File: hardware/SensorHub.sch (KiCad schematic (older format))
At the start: 38 parts, among them IC1 VEML6070, IC2 LT3652EMSE, IC3 BME680, IC4 BH1726, IC5 MCP9808, M1 ParticleArgon, SW1 ENABLE, X1 WIND, X2 SOLAR

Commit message: Release hardware version 1.2
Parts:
- L1: Mfr. No. IDC2512ER330M -> IDC2512ER220M; Order Number 70-IDC2512ER330M -> 70-IDC2512ER220M
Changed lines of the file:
@@
 F 3 "https://www.mouser.de/datasheet/2/427/idc2512-1762893.pdf" H 3700 2650 50  0001 C CNN
 F 4 "Vishay / Dale" V 3981 2650 50  0001 C CNN "Mfr."
-F 5 "IDC2512ER330M" V 3890 2650 50  0001 C CNN "Mfr. No."
+F 5 "IDC2512ER220M" V 3890 2650 50  0001 C CNN "Mfr. No."
 F 6 "Mouser" H 3700 2650 50  0001 C CNN "Distributor"
-F 7 "70-IDC2512ER330M" H 3700 2650 50  0001 C CNN "Order Number"
+F 7 "70-IDC2512ER220M" H 3700 2650 50  0001 C CNN "Order Number"
 	1    3700 2650
 	0    1    1    0

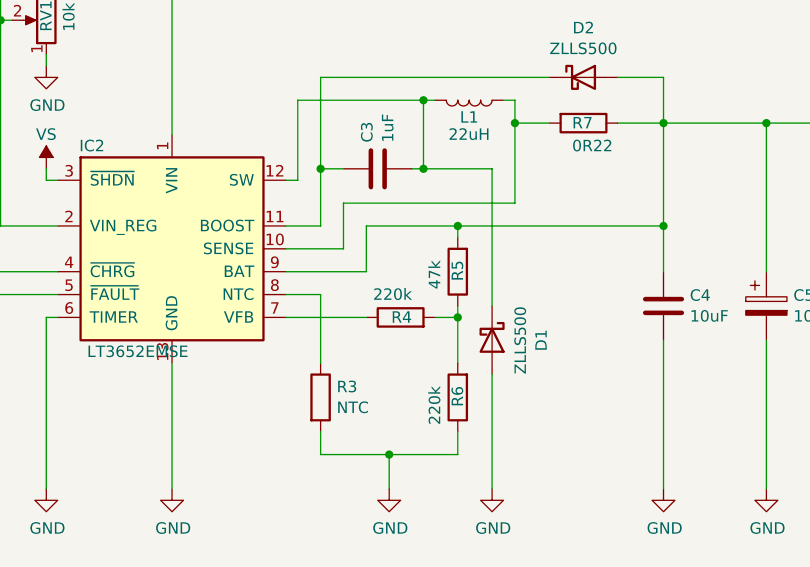
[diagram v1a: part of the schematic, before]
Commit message: - Change the values of the three feedback resistors ('R4', 'R5' and 'R6')
Signed-off-by: Daniel Kampert <DanielKampert@kampis-elektroecke.de>
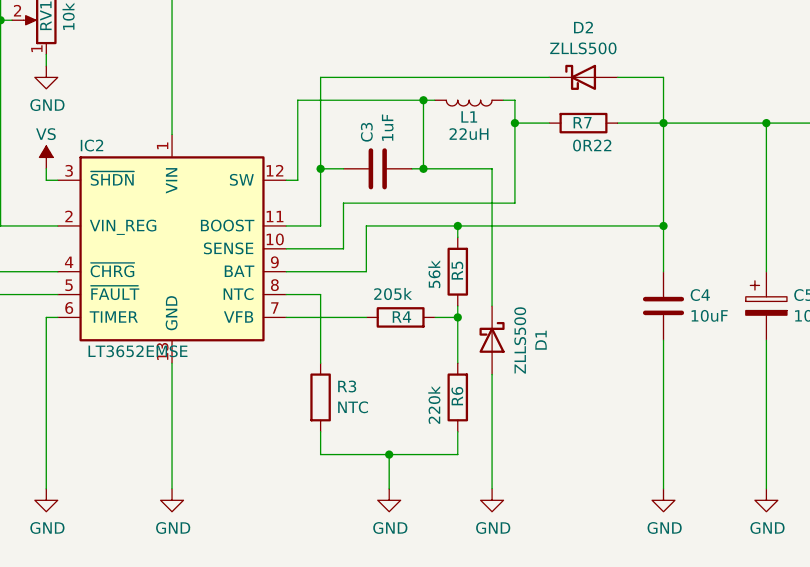
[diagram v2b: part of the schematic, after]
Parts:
- R4: value 220k -> 205k; Mfr. TE Connectivity -> Rohm Semiconductor; Mfr. No. CRGP0805F220K -> KTR10EZPF2053; Order Number 279-CRGP0805F220K -> 755-KTR10EZPF2053
- R5: value 47k -> 56k; Mfr. TE Connectivity -> Rohm Semiconductor; Mfr. No. CRGP0805F47K -> KTR10EZPF5602; Order Number 279-CRGP0805F47K -> 755-KTR10EZPF5602
- R6: Mfr. TE Connectivity -> Bourns; Mfr. No. CRGP0805F220K -> CHV0805-FX-2203ELF; Order Number 279-CRGP0805F220K -> 652-CHV0805FX2203ELF
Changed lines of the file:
@@
 P 3400 3600
 F 0 "R4" V 3400 3550 50  0000 L CNN
-F 1 "220k" V 3500 3550 50  0000 L CNN
+F 1 "205k" V 3500 3550 50  0000 L CNN
 F 2 "Resistor_SMD:R_0805_2012Metric_Pad1.15x1.40mm_HandSolder" V 3330 3600 50  0001 C CNN
-F 3 "~" H 3400 3600 50  0001 C CNN
-F 4 "TE Connectivity" H 3400 3600 50  0001 C CNN "Mfr."
-F 5 "CRGP0805F220K" H 3400 3600 50  0001 C CNN "Mfr. No."
+F 3 "https://www.mouser.de/datasheet/2/348/ktr-e-1139187.pdf" H 3400 3600 50  0001 C CNN
+F 4 "Rohm Semiconductor" H 3400 3600 50  0001 C CNN "Mfr."
+F 5 "KTR10EZPF2053" H 3400 3600 50  0001 C CNN "Mfr. No."
 F 6 "Mouser" H 3400 3600 50  0001 C CNN "Distributor"
-F 7 "279-CRGP0805F220K" H 3400 3600 50  0001 C CNN "Order Number"
+F 7 "755-KTR10EZPF2053" H 3400 3600 50  0001 C CNN "Order Number"
 	1    3400 3600
 	0    -1   -1   0
@@
 P 3650 3400
 F 0 "R5" V 3650 3350 50  0000 L CNN
-F 1 "47k" V 3750 3350 50  0000 L CNN
+F 1 "56k" V 3750 3350 50  0000 L CNN
 F 2 "Resistor_SMD:R_0805_2012Metric_Pad1.15x1.40mm_HandSolder" V 3580 3400 50  0001 C CNN
-F 3 "~" H 3650 3400 50  0001 C CNN
-F 4 "TE Connectivity" H 3650 3400 50  0001 C CNN "Mfr."
-F 5 "CRGP0805F47K" H 3650 3400 50  0001 C CNN "Mfr. No."
+F 3 "https://www.mouser.de/datasheet/2/348/ktr-e-1139187.pdf" H 3650 3400 50  0001 C CNN
+F 4 "Rohm Semiconductor" H 3650 3400 50  0001 C CNN "Mfr."
+F 5 "KTR10EZPF5602" H 3650 3400 50  0001 C CNN "Mfr. No."
 F 6 "Mouser" H 3650 3400 50  0001 C CNN "Distributor"
-F 7 "279-CRGP0805F47K" H 3650 3400 50  0001 C CNN "Order Number"
+F 7 "755-KTR10EZPF5602" H 3650 3400 50  0001 C CNN "Order Number"
 	1    3650 3400
 	-1   0    0    1
@@
 F 1 "220k" V 3750 3900 50  0000 L CNN
 F 2 "Resistor_SMD:R_0805_2012Metric_Pad1.15x1.40mm_HandSolder" V 3580 3950 50  0001 C CNN
-F 3 "~" H 3650 3950 50  0001 C CNN
-F 4 "TE Connectivity" H 3650 3950 50  0001 C CNN "Mfr."
-F 5 "CRGP0805F220K" H 3650 3950 50  0001 C CNN "Mfr. No."
+F 3 "https://www.mouser.de/ProductDetail/Bourns/CHV0805-FX-2203ELF?qs=m3kjewahW8RZW%252Bu5iRLQQg%3D%3D" H 3650 3950 50  0001 C CNN
+F 4 "Bourns" H 3650 3950 50  0001 C CNN "Mfr."
+F 5 "CHV0805-FX-2203ELF" H 3650 3950 50  0001 C CNN "Mfr. No."
 F 6 "Mouser" H 3650 3950 50  0001 C CNN "Distributor"
-F 7 "279-CRGP0805F220K" H 3650 3950 50  0001 C CNN "Order Number"
+F 7 "652-CHV0805FX2203ELF" H 3650 3950 50  0001 C CNN "Order Number"
 	1    3650 3950
 	-1   0    0    1
@@
 The voltage divider is designed\nfor a 17.8 V solar panel.
 $Comp
-L power:GND #PWR?
+L power:GND #PWR0104
 U 1 1 5F0D963C
 P 1850 4350
-F 0 "#PWR?" H 1850 4100 50  0001 C CNN
+F 0 "#PWR0104" H 1850 4100 50  0001 C CNN
 F 1 "GND" H 1855 4177 50  0000 C CNN
 F 2 "" H 1850 4350 50  0001 C CNN
@@
 	1850 3600 1850 4350
 $Comp
-L power:GND #PWR?
+L power:GND #PWR0105
 U 1 1 5F0EDDBF
 P 3350 4350
-F 0 "#PWR?" H 3350 4100 50  0001 C CNN
+F 0 "#PWR0105" H 3350 4100 50  0001 C CNN
 F 1 "GND" H 3355 4177 50  0000 C CNN
 F 2 "" H 3350 4350 50  0001 C CNN

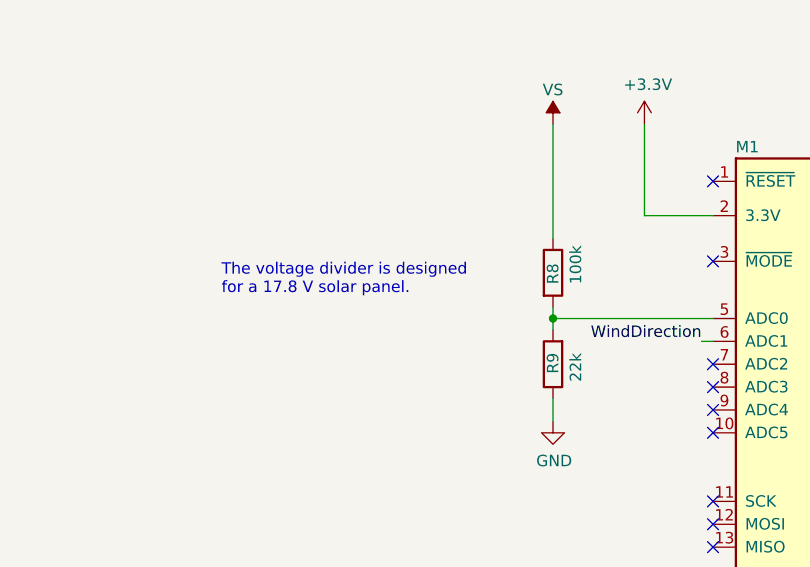
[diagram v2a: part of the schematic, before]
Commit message: Change values for 'R8' and 'R9' to support 20 V solar cells
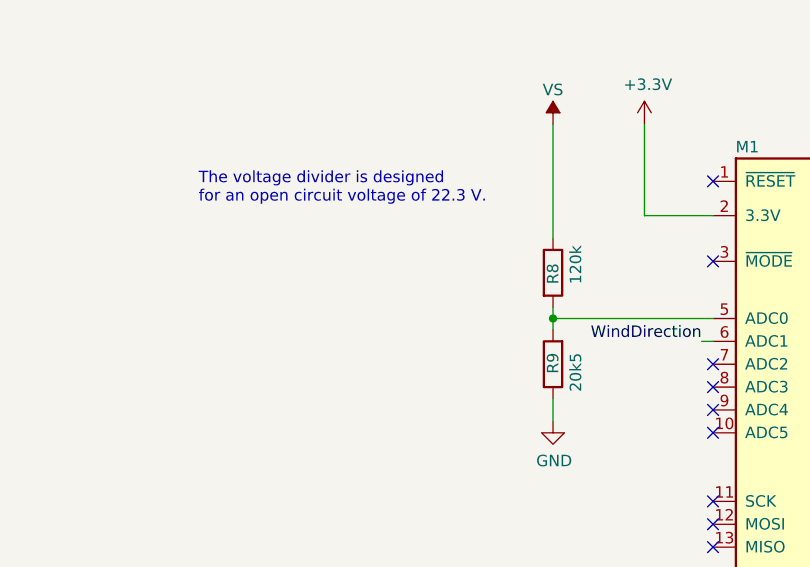
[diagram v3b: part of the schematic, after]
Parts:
- R3: Order Number 81-NXRT15XH103FA5B040 -> 81-NXRT15XH103FA5B40
- R8: value 100k -> 120k; Mfr. Vishay / Draloric -> Rohm Semiconductor; Mfr. No. TNPW0805100KBYEA -> KTR10EZPF1203; Order Number 71-TNPW0805100KBYEA -> 755-KTR10EZPF1203
- R9: value 22k -> 20k5; Mfr. Vishay / Dale -> ROHM Semiconductor; Mfr. No. TNPW080522K0BEEA -> KTR10EZPF2052; Order Number 71-TNPW080522K0BEEA -> 755-KTR10EZPF2052
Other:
- note added: "The voltage divider is designed\nfor an open circuit voltage of 22.3 V."
- note removed: "The voltage divider is designed\nfor a 17.8 V solar panel."

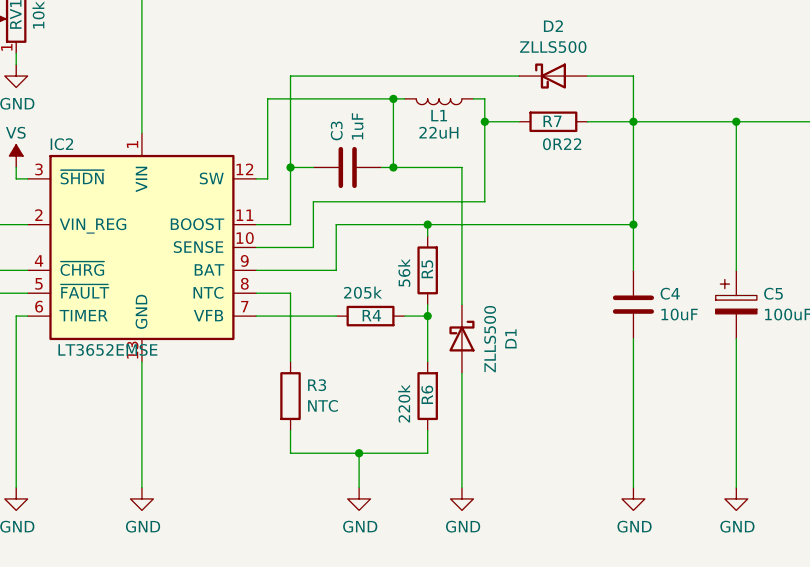
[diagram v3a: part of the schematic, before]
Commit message: - Change 'R5' to 60.4k Ohms
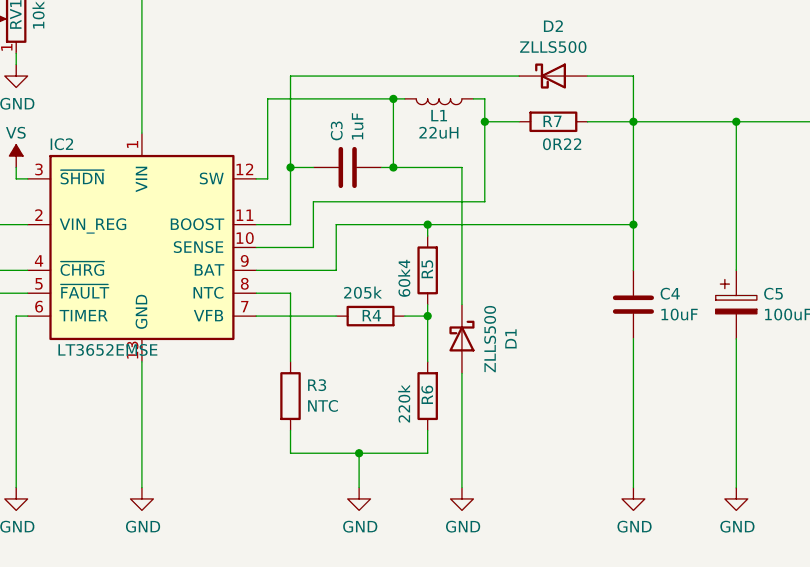
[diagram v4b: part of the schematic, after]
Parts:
- R5: value 56k -> 60k4; Mfr. No. KTR10EZPF5602 -> KTR10EZPF6042; Order Number 755-KTR10EZPF5602 -> 755-KTR10EZPF6042
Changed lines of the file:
@@
 P 3650 3400
 F 0 "R5" V 3650 3350 50  0000 L CNN
-F 1 "56k" V 3750 3350 50  0000 L CNN
+F 1 "60k4" V 3750 3350 50  0000 L CNN
 F 2 "Resistor_SMD:R_0805_2012Metric_Pad1.15x1.40mm_HandSolder" V 3580 3400 50  0001 C CNN
 F 3 "https://www.mouser.de/datasheet/2/348/ktr-e-1139187.pdf" H 3650 3400 50  0001 C CNN
 F 4 "Rohm Semiconductor" H 3650 3400 50  0001 C CNN "Mfr."
-F 5 "KTR10EZPF5602" H 3650 3400 50  0001 C CNN "Mfr. No."
+F 5 "KTR10EZPF6042" H 3650 3400 50  0001 C CNN "Mfr. No."
 F 6 "Mouser" H 3650 3400 50  0001 C CNN "Distributor"
-F 7 "755-KTR10EZPF5602" H 3650 3400 50  0001 C CNN "Order Number"
+F 7 "755-KTR10EZPF6042" H 3650 3400 50  0001 C CNN "Order Number"
 	1    3650 3400
 	-1   0    0    1
